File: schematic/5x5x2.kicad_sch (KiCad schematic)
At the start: 178 parts, among them J1 SW Debug, J10 Conn_01x03_Female, J11 Conn_01x03_Male, J12 Conn_01x03_Male, J13 Conn_01x03_Female, J14 Conn_01x03_Female, J15 Conn_01x03_Male, J16 Conn_01x03_Female, J2 USB_C_Receptacle_USB2.0, J3 Conn_01x03_Male, J4 Conn_01x03_Male, J5 Conn_01x03_Female, J6 Conn_01x03_Female, J7 Conn_01x03_Male, J8 Conn_01x03_Male, J9 Conn_01x03_Female, SW1 SW, SW11 SW, SW12 SW, SW13 SW, SW14 SW, SW15 SW, SW21 SW, SW22 SW, SW23 SW, SW24 SW, SW25 SW, SW31 SW, SW32 SW, SW33 SW, SW34 SW, SW35 SW, SW41 SW, SW42 SW, SW43 SW, SW44 SW, SW45 SW, SW51 SW, SW52 SW, SW53 SW, SW54 SW, SW55 SW, SW6 ALPS_EC11, U1 SRV0504, U2 STM32F103C8, U3 LD1117S33CTR, Y1 16M

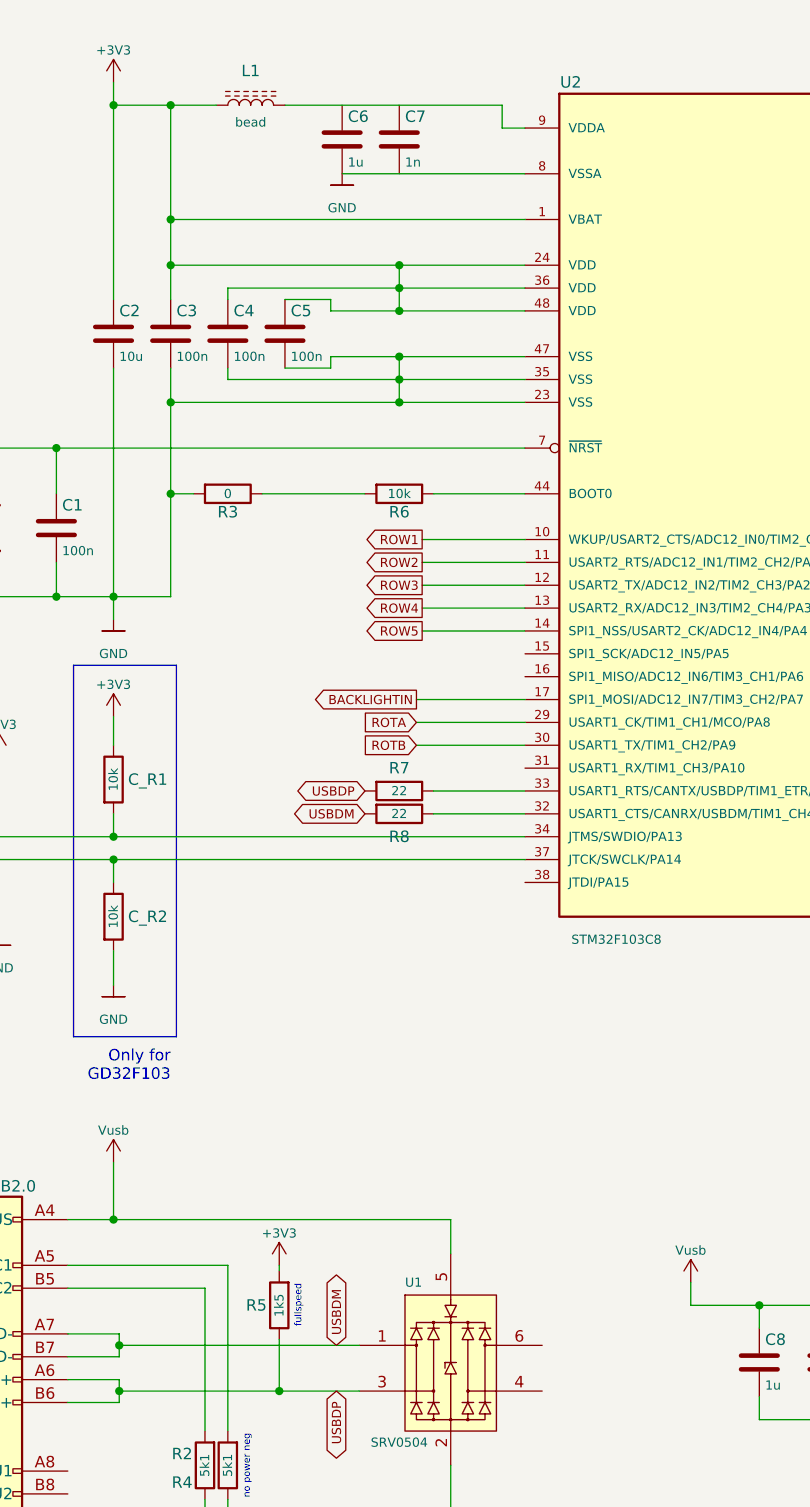
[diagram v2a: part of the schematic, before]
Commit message: Adjusted to 4 layer board
- USB interface is most important, lets route that first.

- leds interconnect will mess with everybody, so push those to the
  internal layer.

- do away with quirky 45 degree placing
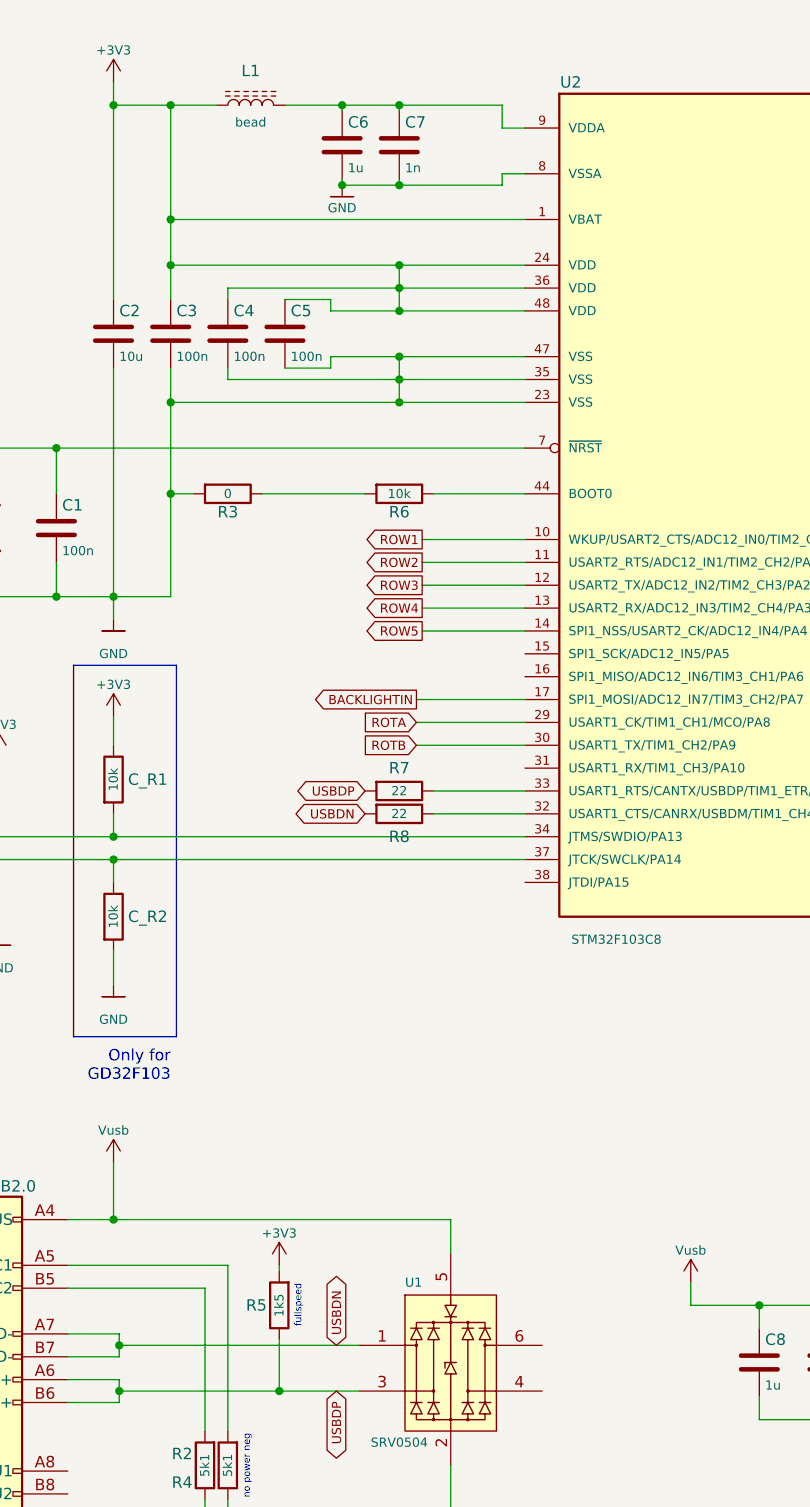
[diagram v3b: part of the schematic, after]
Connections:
- net GND: now also C7.2
- net at C6.1: now also C7.1, L1.2, U2.9 (VDDA)
- net USBDM renamed USBDN
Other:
- moved on the sheet: C6, C7
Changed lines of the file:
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@@
   (junction (at 353.695 88.265) (diameter 0) (color 0 0 0 0)
   )
+  (junction (at 87.63 35.56) (diameter 0) (color 0 0 0 0)
+  )
   (junction (at 55.88 107.95) (diameter 0) (color 0 0 0 0)
   )
@@
   (junction (at 310.515 131.445) (diameter 0) (color 0 0 0 0)
   )
+  (junction (at 87.63 26.67) (diameter 0) (color 0 0 0 0)
+  )
   (junction (at 334.645 188.595) (diameter 0) (color 0 0 0 0)
   )
@@
   (junction (at 116.84 265.43) (diameter 0) (color 0 0 0 0)
   )
+  (junction (at 81.28 35.56) (diameter 0) (color 0 0 0 0)
+  )
   (junction (at 209.55 77.47) (diameter 0) (color 0 0 0 0)
   )
@@
   (junction (at 366.395 201.295) (diameter 0) (color 0 0 0 0)
   )
+  (junction (at 81.28 26.67) (diameter 0) (color 0 0 0 0)
+  )
   (junction (at 62.23 59.69) (diameter 0) (color 0 0 0 0)
   )
@@
     (stroke (width 0) (type default) (color 0 0 0 0))
   )
-  (wire (pts (xy 74.93 26.67) (xy 99.06 26.67))
+  (wire (pts (xy 74.93 26.67) (xy 81.28 26.67))
     (stroke (width 0) (type default) (color 0 0 0 0))
   )
@@
     (stroke (width 0) (type default) (color 0 0 0 0))
   )
-  (wire (pts (xy 81.28 34.29) (xy 101.6 34.29))
-    (stroke (width 0) (type default) (color 0 0 0 0))
-  )
   (wire (pts (xy 182.88 260.35) (xy 180.34 260.35))
     (stroke (width 0) (type default) (color 0 0 0 0))
@@
     (stroke (width 0) (type default) (color 0 0 0 0))
   )
+  (wire (pts (xy 81.28 26.67) (xy 87.63 26.67))
+    (stroke (width 0) (type default) (color 0 0 0 0))
+  )
   (wire (pts (xy 332.105 45.085) (xy 353.695 45.085))
     (stroke (width 0) (type default) (color 0 0 0 0))
@@
     (stroke (width 0) (type default) (color 0 0 0 0))
   )
+  (wire (pts (xy 99.06 35.56) (xy 87.63 35.56))
+    (stroke (width 0) (type default) (color 0 0 0 0))
+  )
   (wire (pts (xy 315.595 213.995) (xy 315.595 211.455))
     (stroke (width 0) (type default) (color 0 0 0 0))
@@
     (stroke (width 0) (type default) (color 0 0 0 0))
   )
+  (wire (pts (xy 87.63 35.56) (xy 81.28 35.56))
+    (stroke (width 0) (type default) (color 0 0 0 0))
+  )
   (wire (pts (xy 144.78 247.65) (xy 142.24 247.65))
     (stroke (width 0) (type default) (color 0 0 0 0))
@@
     (stroke (width 0) (type default) (color 0 0 0 0))
   )
+  (wire (pts (xy 81.28 34.925) (xy 81.28 35.56))
+    (stroke (width 0) (type default) (color 0 0 0 0))
+  )
   (wire (pts (xy 184.785 160.02) (xy 184.785 157.48))
     (stroke (width 0) (type default) (color 0 0 0 0))
@@
     (stroke (width 0) (type default) (color 0 0 0 0))
   )
+  (wire (pts (xy 99.06 34.29) (xy 99.06 35.56))
+    (stroke (width 0) (type default) (color 0 0 0 0))
+  )
   (wire (pts (xy 62.23 26.67) (xy 67.31 26.67))
     (stroke (width 0) (type default) (color 0 0 0 0))
@@
     (stroke (width 0) (type default) (color 0 0 0 0))
   )
+  (wire (pts (xy 87.63 26.67) (xy 87.63 27.305))
+    (stroke (width 0) (type default) (color 0 0 0 0))
+  )
   (wire (pts (xy 116.84 265.43) (xy 154.94 265.43))
     (stroke (width 0) (type default) (color 0 0 0 0))
@@
     (stroke (width 0) (type default) (color 0 0 0 0))
   )
+  (wire (pts (xy 87.63 26.67) (xy 99.06 26.67))
+    (stroke (width 0) (type default) (color 0 0 0 0))
+  )
   (wire (pts (xy 310.515 109.22) (xy 332.105 109.22))
     (stroke (width 0) (type default) (color 0 0 0 0))
@@
     (stroke (width 0) (type default) (color 0 0 0 0))
   )
+  (wire (pts (xy 87.63 34.925) (xy 87.63 35.56))
+    (stroke (width 0) (type default) (color 0 0 0 0))
+  )
+  (wire (pts (xy 101.6 34.29) (xy 99.06 34.29))
+    (stroke (width 0) (type default) (color 0 0 0 0))
+  )
   (wire (pts (xy 290.195 188.595) (xy 296.545 188.595))
     (stroke (width 0) (type default) (color 0 0 0 0))
@@
     (stroke (width 0) (type default) (color 0 0 0 0))
   )
+  (wire (pts (xy 81.28 26.67) (xy 81.28 27.305))
+    (stroke (width 0) (type default) (color 0 0 0 0))
+  )
   (wire (pts (xy 62.23 59.69) (xy 62.23 55.88))
     (stroke (width 0) (type default) (color 0 0 0 0))
@@
     )
   )
-  (global_label "USBDM" (shape bidirectional) (at 83.82 105.41 180) (fields_autoplaced)
+  (global_label "USBDN" (shape bidirectional) (at 83.82 105.41 180) (fields_autoplaced)
     (effects (font (size 1.016 1.016)) (justify right))
-    (property "Intersheet References" "${INTERSHEET_REFS}" (id 0) (at 76.6645 105.3465 0)
+    (property "Intersheet References" "${INTERSHEET_REFS}" (id 0) (at 76.7612 105.3465 0)
       (effects (font (size 1.016 1.016)) (justify right) hide)
     )
@@
     )
   )
-  (global_label "USBDM" (shape bidirectional) (at 80.645 164.465 90) (fields_autoplaced)
+  (global_label "USBDN" (shape bidirectional) (at 80.645 164.465 90) (fields_autoplaced)
     (effects (font (size 1.016 1.016)) (justify left))
-    (property "Intersheet References" "${INTERSHEET_REFS}" (id 0) (at 80.7085 157.3095 90)
+    (property "Intersheet References" "${INTERSHEET_REFS}" (id 0) (at 80.5815 157.4062 90)
       (effects (font (size 1.016 1.016)) (justify left) hide)
     )
@@
     (pin "2")
   )
-  (symbol (lib_id "Device:C") (at 81.28 30.48 0) (unit 1)
+  (symbol (lib_id "Device:C") (at 81.28 31.115 0) (unit 1)
     (in_bom yes) (on_board yes)
-    (property "Reference" "C6" (id 0) (at 81.915 27.94 0)
+    (property "Reference" "C6" (id 0) (at 81.915 28.575 0)
       (effects (font (size 1.27 1.27)) (justify left))
     )
-    (property "Value" "1u" (id 1) (at 81.915 33.02 0)
+    (property "Value" "1u" (id 1) (at 81.915 33.655 0)
       (effects (font (size 1.016 1.016)) (justify left))
     )
-    (property "Footprint" "Capacitor_SMD:C_1206_3216Metric" (id 2) (at 82.2452 34.29 0)
+    (property "Footprint" "Capacitor_SMD:C_1206_3216Metric" (id 2) (at 82.2452 34.925 0)
       (effects (font (size 1.27 1.27)) hide)
     )
-    (property "Datasheet" "~" (id 3) (at 81.28 30.48 0)
+    (property "Datasheet" "~" (id 3) (at 81.28 31.115 0)
       (effects (font (size 1.27 1.27)) hide)
     )
@@
     (pin "E")
   )
-  (symbol (lib_id "usb:GND") (at 81.28 34.29 0) (unit 1)
+  (symbol (lib_id "usb:GND") (at 81.28 35.56 0) (unit 1)
     (in_bom yes) (on_board yes)
-    (property "Reference" "#PWR010" (id 0) (at 81.28 40.64 0)
+    (property "Reference" "#PWR010" (id 0) (at 81.28 41.91 0)
       (effects (font (size 1.27 1.27)) hide)
     )
@@
       (effects (font (size 1.016 1.016)))
     )
-    (property "Footprint" "" (id 2) (at 81.28 34.29 0)
+    (property "Footprint" "" (id 2) (at 81.28 35.56 0)
       (effects (font (size 1.524 1.524)))
     )
-    (property "Datasheet" "" (id 3) (at 81.28 34.29 0)
+    (property "Datasheet" "" (id 3) (at 81.28 35.56 0)
       (effects (font (size 1.524 1.524)))
     )
@@
     (pin "2")
   )
-  (symbol (lib_id "Device:C") (at 87.63 30.48 0) (unit 1)
+  (symbol (lib_id "Device:C") (at 87.63 31.115 0) (unit 1)
     (in_bom yes) (on_board yes)
-    (property "Reference" "C7" (id 0) (at 88.265 27.94 0)
+    (property "Reference" "C7" (id 0) (at 88.265 28.575 0)
       (effects (font (size 1.27 1.27)) (justify left))
     )
-    (property "Value" "1n" (id 1) (at 88.265 33.02 0)
+    (property "Value" "1n" (id 1) (at 88.265 33.655 0)
       (effects (font (size 1.016 1.016)) (justify left))
     )
-    (property "Footprint" "Capacitor_SMD:C_0805_2012Metric" (id 2) (at 88.5952 34.29 0)
+    (property "Footprint" "Capacitor_SMD:C_0805_2012Metric" (id 2) (at 88.5952 34.925 0)
       (effects (font (size 1.27 1.27)) hide)
     )
-    (property "Datasheet" "~" (id 3) (at 87.63 30.48 0)
+    (property "Datasheet" "~" (id 3) (at 87.63 31.115 0)
       (effects (font (size 1.27 1.27)) hide)
     )

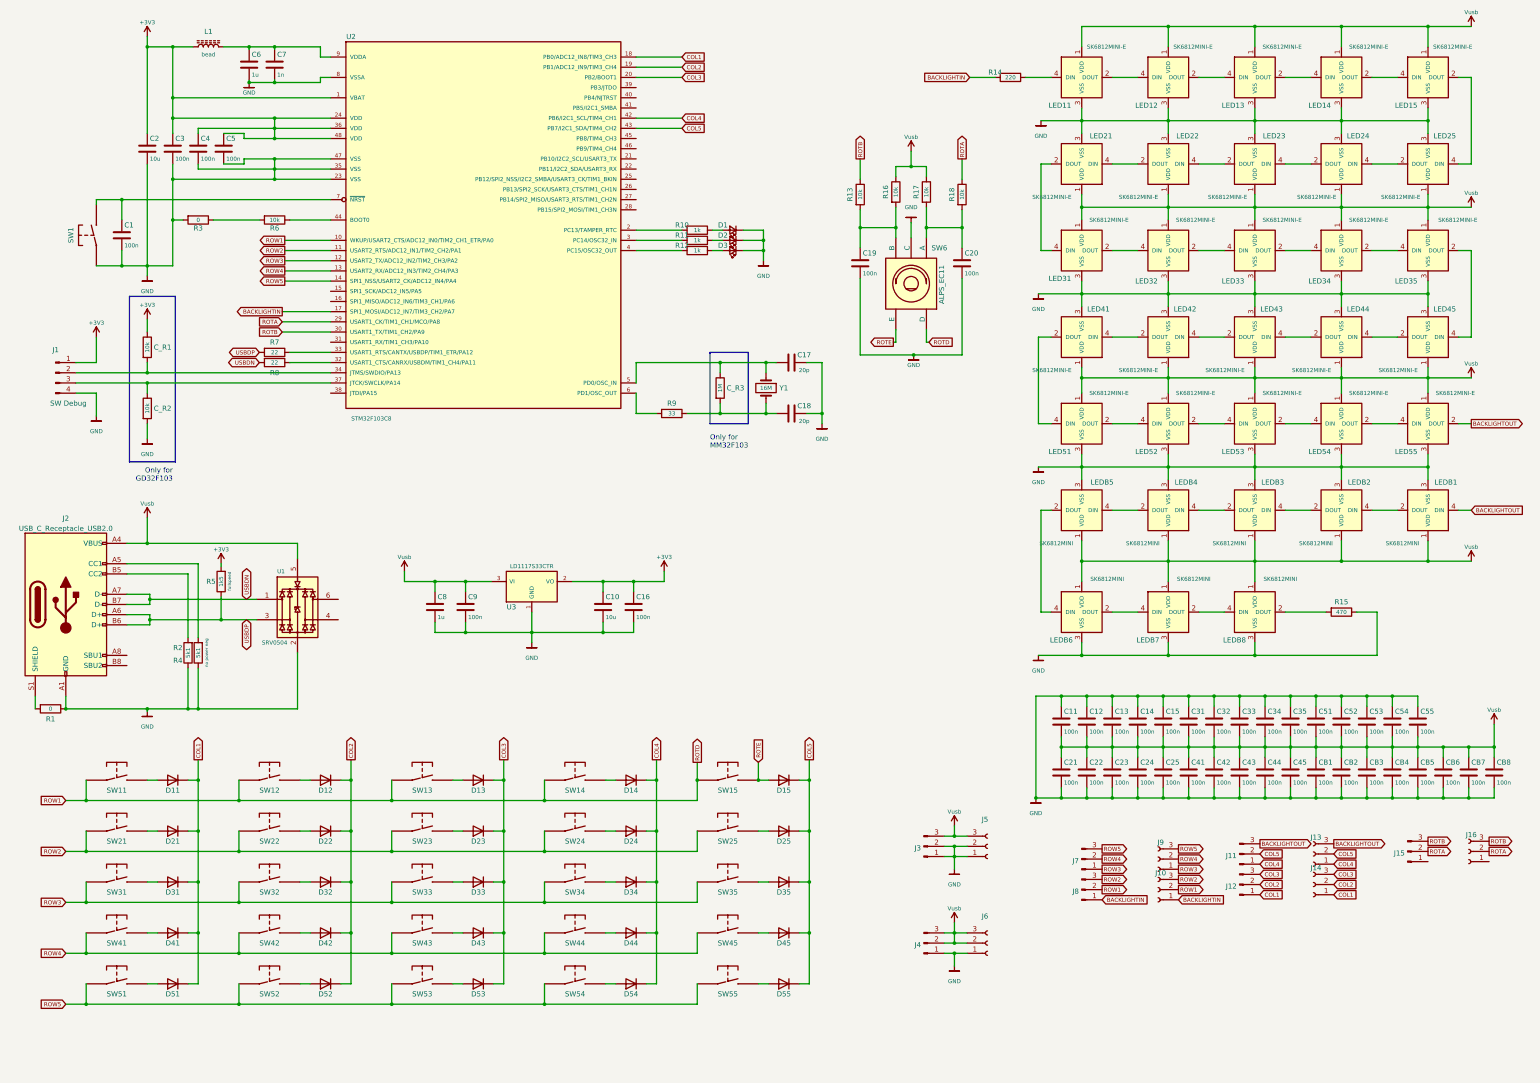
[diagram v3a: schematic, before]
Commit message: Routed all remaining parts.
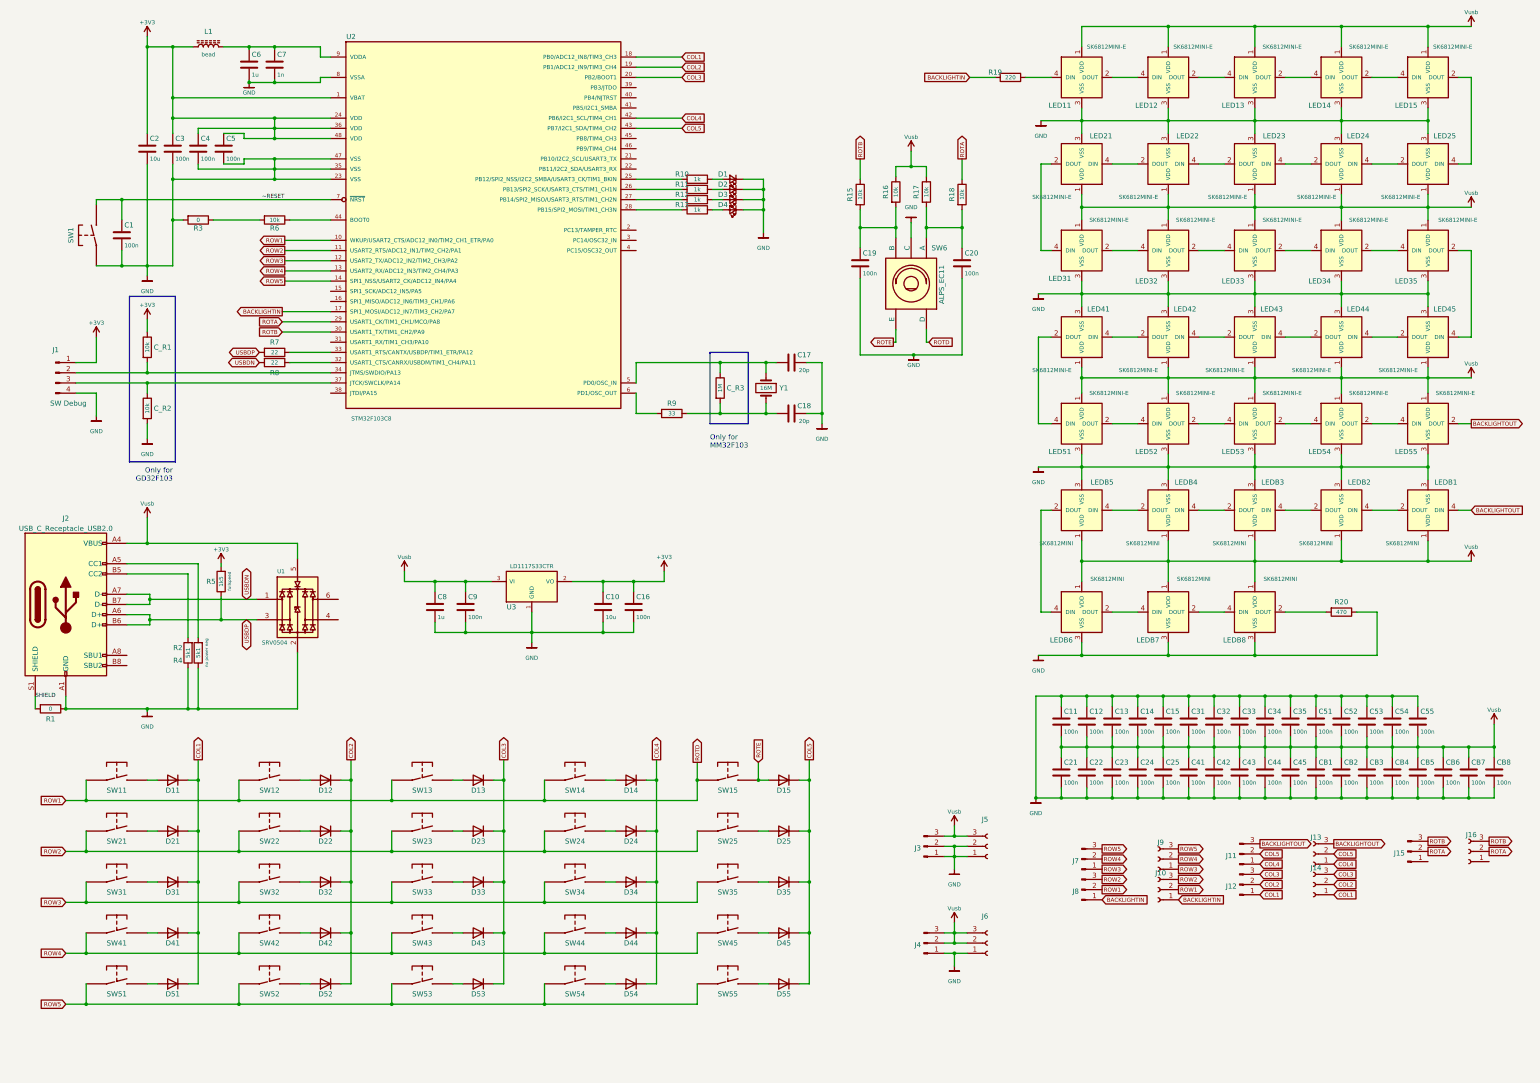
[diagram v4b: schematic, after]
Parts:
- added D4: Led_Small, LED_SMD:LED_0805_2012Metric, symbol Device:LED_Small
- added R13: 1k, Resistor_SMD:R_0805_2012Metric, symbol Device:R
- SW1: footprint Connector_PinSocket_1.27mm:PinSocket_1x02_P1.27mm_Vertical -> Button_Switch_SMD:SW_SPST_FSMSM
- renumbered R13 to R15, R14 to R19, R15 to R20
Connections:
- net GND: now also D4.1 (K)
- net at R11.2: now also U2.26 (PB13/SPI2_SCK/USART3_CTS/TIM1_CH1N); no longer U2.3 (PC14/OSC32_IN)
- net at R12.2: now also U2.27 (PB14/SPI2_MISO/USART3_RTS/TIM1_CH2N); no longer U2.4 (PC15/OSC32_OUT)
- net SHIELD: now reaches J2.S1 (SHIELD), R1.2
- net ~RESET: now reaches C1.1, SW1.2, U2.7 (~{NRST})
- net at U2.2 (PC13/TAMPER_RTC): no longer R10.2
- net at U2.25 (PB12/SPI2_NSS/I2C2_SMBA/USART3_CK/TIM1_BKIN): now also R10.2
- net at U2.28 (PB15/SPI2_MOSI/TIM1_CH3N): now also R13.2
- new net: D4.2 (A), R13.1
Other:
- moved on the sheet: D1, D2, D3, R10, R11, R12
